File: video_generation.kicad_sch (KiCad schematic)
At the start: 53 parts, among them J12 28L22, J13 74LS86, J14 74LS166, J15 74LS161, K0000 74LS00, K10 74LS08, K11 74LS273, K12 74LS273, K14 74LS10, K15 74LS04, U14 74LS00, U2 74LS32, U3 74LS08, U4 74LS04, U5 74LS00

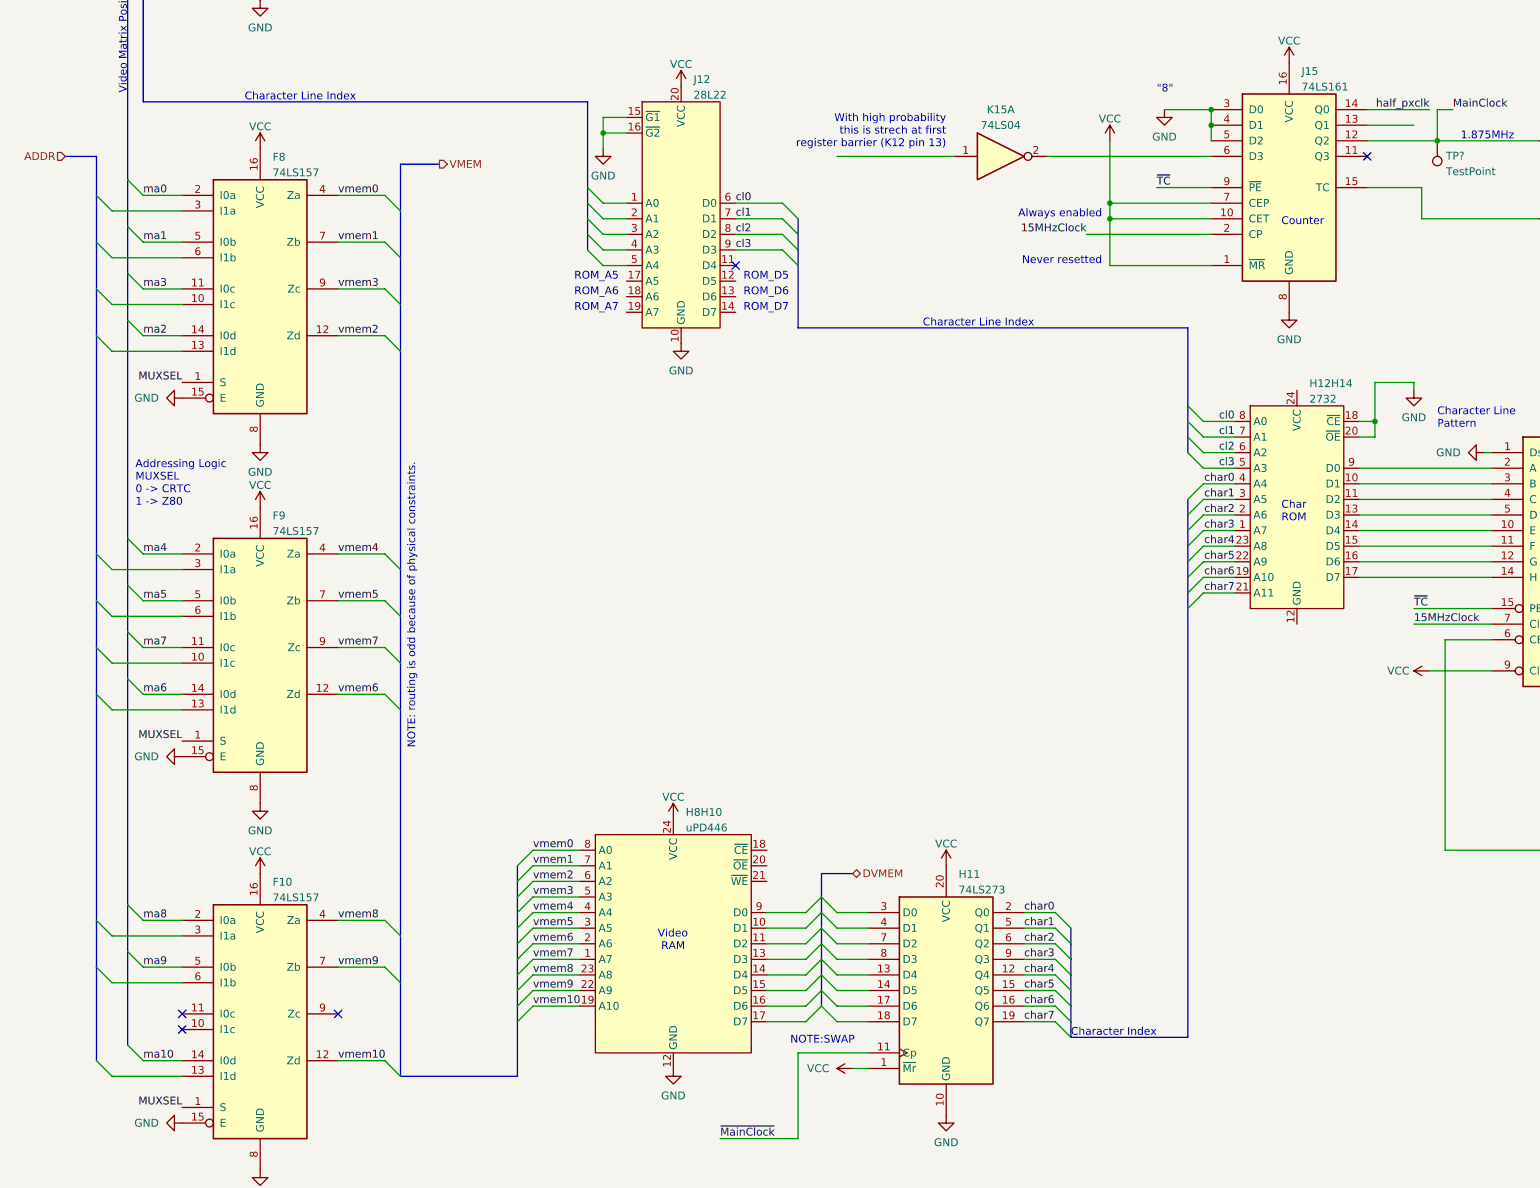
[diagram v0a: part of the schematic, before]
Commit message: Discovered WE and OE signals for video memories, plus others
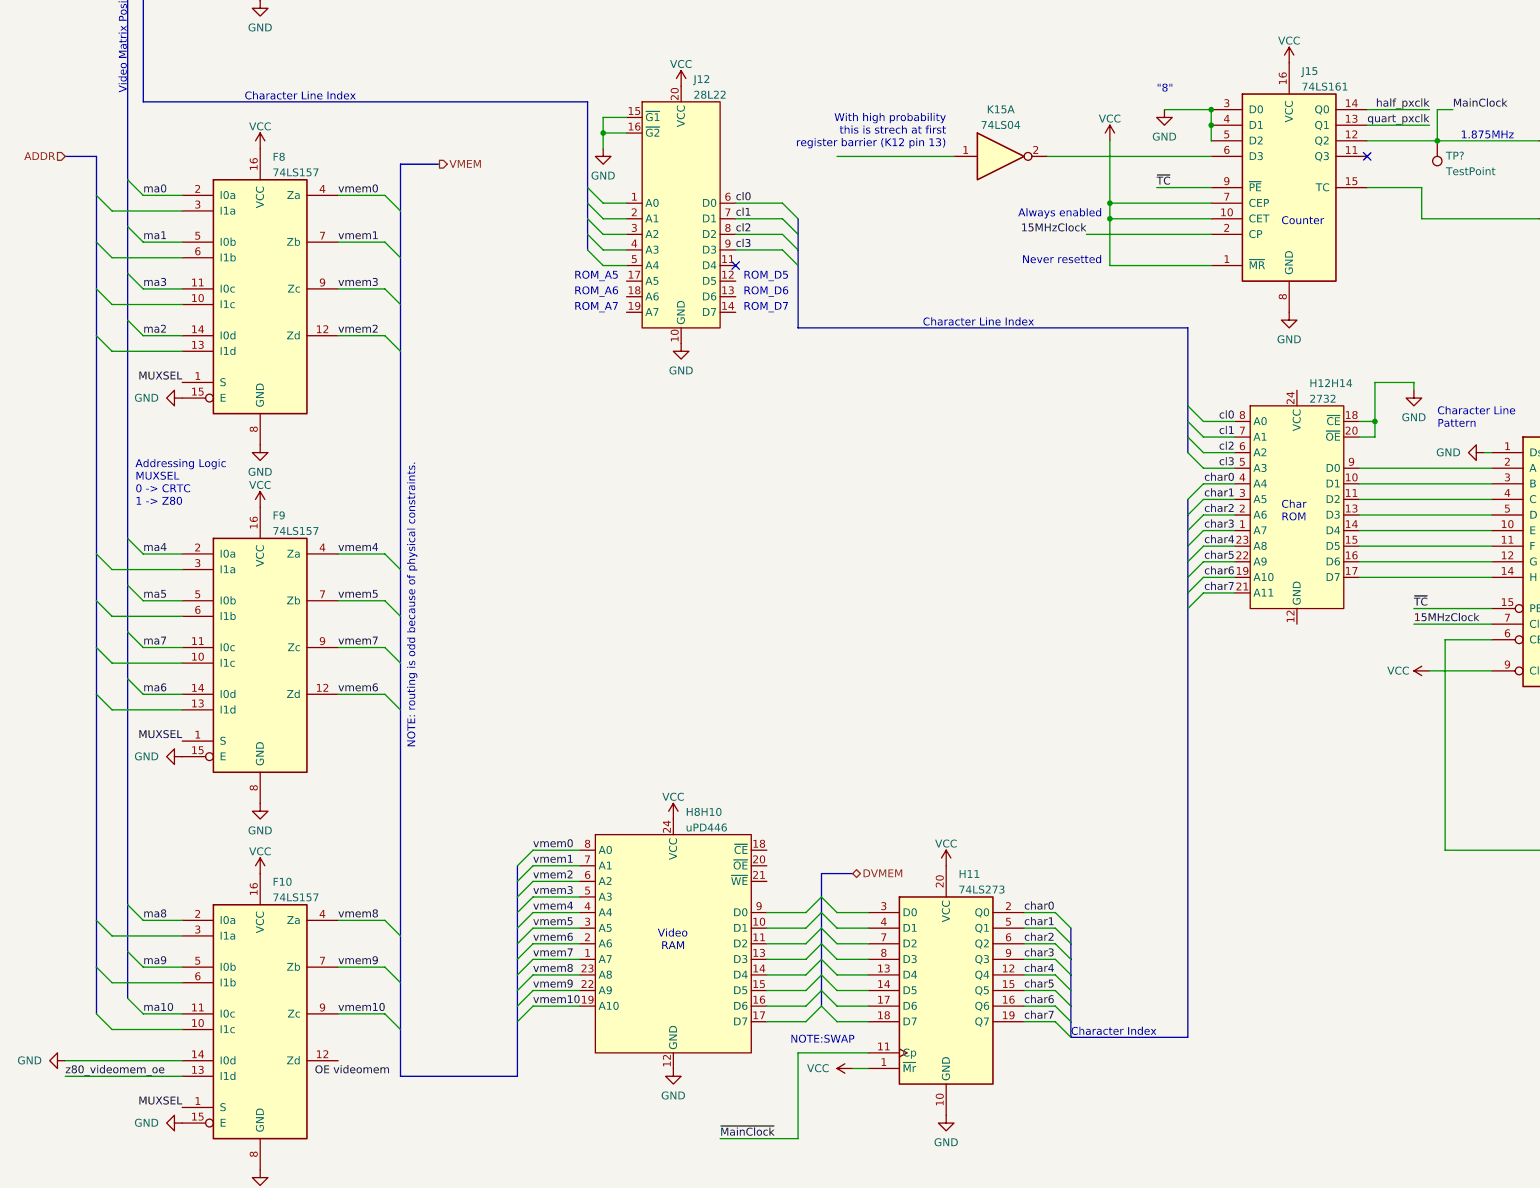
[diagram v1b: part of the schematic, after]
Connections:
- net GND: now also F10.14 (I0d)
- net ma10: now also F10.11 (I0c); no longer F10.14 (I0d)
- net vmem10: now also F10.9 (Zc); no longer F10.12 (Zd)
- net quart_pxclk: now reaches J15.13 (Q1)
- net z80_videomem_oe: now reaches F10.13 (I1d)
- no-connect marks 30 -> 27
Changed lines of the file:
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@@
   (no_connect (at 252.73 34.29))
   (no_connect (at 265.43 29.21))
-  (no_connect (at 39.37 256.54))
   (no_connect (at 374.65 143.51))
   (no_connect (at 495.3 228.6))
@@
   (no_connect (at 38.1 62.23))
   (no_connect (at 38.1 59.69))
-  (no_connect (at 64.77 254))
-  (no_connect (at 39.37 254))
   (no_connect (at 458.47 226.06))
   (no_connect (at 458.47 231.14))
@@
     (stroke (width 0) (type default))
   )
-  (bus_entry (at 72.39 261.62) (size 2.54 2.54)
+  (bus_entry (at 72.39 254) (size 2.54 2.54)
     (stroke (width 0) (type default))
   )
@@
     (stroke (width 0) (type default))
   )
-  (bus_entry (at 30.48 259.08) (size 2.54 2.54)
+  (bus_entry (at 30.48 251.46) (size 2.54 2.54)
     (stroke (width 0) (type default))
   )
@@
     (stroke (width 0) (type default))
   )
-  (bus_entry (at 25.4 261.62) (size 2.54 2.54)
+  (bus_entry (at 25.4 254) (size 2.54 2.54)
     (stroke (width 0) (type default))
   )
@@
     (stroke (width 0) (type default))
   )
-  (wire (pts (xy 27.94 264.16) (xy 39.37 264.16))
+  (wire (pts (xy 27.94 256.54) (xy 39.37 256.54))
     (stroke (width 0) (type default))
   )
@@
     (stroke (width 0) (type default))
   )
-  (wire (pts (xy 64.77 261.62) (xy 72.39 261.62))
+  (wire (pts (xy 64.77 254) (xy 72.39 254))
     (stroke (width 0) (type default))
   )
@@
     (stroke (width 0) (type default))
   )
-  (bus (pts (xy 30.48 243.84) (xy 30.48 259.08))
+  (bus (pts (xy 30.48 243.84) (xy 30.48 251.46))
     (stroke (width 0) (type default))
   )
@@
     (stroke (width 0) (type default))
   )
+  (bus (pts (xy 74.93 256.54) (xy 74.93 264.16))
+    (stroke (width 0) (type default))
+  )
   (wire (pts (xy 231.14 180.34) (xy 252.73 180.34))
     (stroke (width 0) (type default))
@@
     (stroke (width 0) (type default))
   )
-  (bus (pts (xy 74.93 248.92) (xy 74.93 264.16))
+  (bus (pts (xy 74.93 248.92) (xy 74.93 256.54))
     (stroke (width 0) (type default))
   )
@@
     (stroke (width 0) (type default))
   )
+  (wire (pts (xy 20.32 261.62) (xy 39.37 261.62))
+    (stroke (width 0) (type default))
+  )
   (wire (pts (xy 33.02 41.91) (xy 38.1 41.91))
     (stroke (width 0) (type default))
@@
     (stroke (width 0) (type default))
   )
-  (wire (pts (xy 33.02 261.62) (xy 39.37 261.62))
+  (wire (pts (xy 33.02 254) (xy 39.37 254))
     (stroke (width 0) (type default))
   )
@@
     (stroke (width 0) (type default))
   )
+  (wire (pts (xy 20.32 264.16) (xy 39.37 264.16))
+    (stroke (width 0) (type default))
+  )
   (wire (pts (xy 107.95 129.54) (xy 111.76 129.54))
     (stroke (width 0) (type default))
@@
     (stroke (width 0) (type default))
   )
-  (wire (pts (xy 232.41 109.22) (xy 240.03 109.22))
+  (wire (pts (xy 232.41 109.22) (xy 242.57 109.22))
     (stroke (width 0) (type default))
   )
@@
     (stroke (width 0) (type default))
   )
-  (bus (pts (xy 25.4 246.38) (xy 25.4 261.62))
+  (bus (pts (xy 25.4 246.38) (xy 25.4 254))
     (stroke (width 0) (type default))
   )
@@
     (effects (font (size 1.27 1.27)) (justify left bottom))
   )
-  (label "vmem10" (at 64.77 261.62 0) (fields_autoplaced)
+  (label "vmem10" (at 64.77 254 0) (fields_autoplaced)
     (effects (font (size 1.27 1.27)) (justify left bottom))
   )
@@
     (effects (font (size 1.27 1.27)) (justify left bottom))
   )
+  (label "OE videomem" (at 60.96 264.16 0) (fields_autoplaced)
+    (effects (font (size 1.27 1.27)) (justify left bottom))
+  )
   (label "CONTRAST1" (at 247.65 21.59 180) (fields_autoplaced)
     (effects (font (size 1.27 1.27)) (justify right bottom))
@@
     (effects (font (size 1.27 1.27)) (justify left bottom))
   )
+  (label "quart_pxclk" (at 242.57 109.22 180) (fields_autoplaced)
+    (effects (font (size 1.27 1.27)) (justify right bottom))
+  )
   (label "cl0" (at 36.83 69.85 180) (fields_autoplaced)
     (effects (font (size 1.27 1.27)) (justify right bottom))
   )
-  (label "ma10" (at 33.02 261.62 0) (fields_autoplaced)
+  (label "ma10" (at 33.02 254 0) (fields_autoplaced)
+    (effects (font (size 1.27 1.27)) (justify left bottom))
+  )
+  (label "z80_videomem_oe" (at 20.32 264.16 0) (fields_autoplaced)
     (effects (font (size 1.27 1.27)) (justify left bottom))
   )
@@
         )
       )
+    )
+  )
+  (symbol (lib_id "power:GND") (at 20.32 261.62 270) (unit 1)
+    (in_bom yes) (on_board yes) (dnp no)
+    (property "Reference" "#PWR0114" (at 13.97 261.62 0)
+      (effects (font (size 1.27 1.27)) hide)
+    )
+    (property "Value" "GND" (at 16.51 261.62 90)
+      (effects (font (size 1.27 1.27)) (justify right))
+    )
+    (property "Footprint" "" (at 20.32 261.62 0)
+      (effects (font (size 1.27 1.27)) hide)
+    )
+    (property "Datasheet" "" (at 20.32 261.62 0)
+      (effects (font (size 1.27 1.27)) hide)
+    )
+    (pin "1")
+    (instances
+      (project "ceda"
+        (path "/12a6dbe3-008d-4c5b-88f6-9f1c816060be/ce60e45b-d802-4380-8f39-bef3de5fa20e"
+          (reference "#PWR0114") (unit 1)
+        )
+      )

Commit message: Schematics refactoring:
- New sheet reserved to video memory.
- Removed video memory parts inside video_generation.
- Removed video memory parts inside GPIO.
- Generic cleanup to keep all circuits inside each sheet.
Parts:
- removed F10, F8, F9: 74LS157, symbol 74xx:74LS157
- removed H8H10: uPD446, symbol ceda:uPD446
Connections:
- net muxsel is gone; now on net MUXSEL: E12.9 (Cp)
- net dot pattern: now also J14.13 (Qh)
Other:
- note removed: ""8""
- note removed: "Addressing Logic MUXSEL 0 -> CRTC 1 -> Z80"
- note removed: "Character Index"
- note removed: "NOTE: routing is odd because of physical constraints."
- note removed: "TODO: feedback network is missing. Circuit must be something like as dashed lines"
- note removed: "Video Matrix Position"
- note removed: "Video RAM"
- moved on the sheet: C52, C53, C54, D2, D5, E12, H11, H12H14, J12, J13A, J13B, J14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

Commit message: Removed some dangling notes
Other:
- note removed: "Dot Pattern"
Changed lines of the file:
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@@
     (stroke (width 0) (type default))
   )
-  (bus_entry (at 66.04 167.64) (size 2.54 2.54)
-    (stroke (width 0) (type default))
-  )
-  (bus_entry (at 66.04 165.1) (size 2.54 2.54)
-    (stroke (width 0) (type default))
-  )
-  (bus_entry (at 66.04 172.72) (size 2.54 2.54)
-    (stroke (width 0) (type default))
-  )
-  (bus_entry (at 66.04 170.18) (size 2.54 2.54)
-    (stroke (width 0) (type default))
-  )
-  (bus_entry (at 66.04 162.56) (size 2.54 2.54)
-    (stroke (width 0) (type default))
-  )
-  (bus_entry (at 66.04 175.26) (size 2.54 2.54)
+  (bus_entry (at 68.58 167.64) (size 2.54 2.54)
+    (stroke (width 0) (type default))
+  )
+  (bus_entry (at 68.58 165.1) (size 2.54 2.54)
+    (stroke (width 0) (type default))
+  )
+  (bus_entry (at 68.58 172.72) (size 2.54 2.54)
+    (stroke (width 0) (type default))
+  )
+  (bus_entry (at 68.58 170.18) (size 2.54 2.54)
+    (stroke (width 0) (type default))
+  )
+  (bus_entry (at 68.58 162.56) (size 2.54 2.54)
+    (stroke (width 0) (type default))
+  )
+  (bus_entry (at 68.58 175.26) (size 2.54 2.54)
     (stroke (width 0) (type default))
   )
@@
     (stroke (width 0) (type default))
   )
-  (bus_entry (at 66.04 180.34) (size 2.54 2.54)
-    (stroke (width 0) (type default))
-  )
-  (bus_entry (at 66.04 177.8) (size 2.54 2.54)
+  (bus_entry (at 68.58 180.34) (size 2.54 2.54)
+    (stroke (width 0) (type default))
+  )
+  (bus_entry (at 68.58 177.8) (size 2.54 2.54)
     (stroke (width 0) (type default))
   )
@@
     (stroke (width 0) (type default))
   )
-  (wire (pts (xy 60.96 167.64) (xy 66.04 167.64))
+  (wire (pts (xy 60.96 167.64) (xy 68.58 167.64))
     (stroke (width 0) (type default))
   )
@@
     (stroke (width 0) (type default))
   )
-  (bus (pts (xy 68.58 172.72) (xy 68.58 175.26))
+  (bus (pts (xy 71.12 172.72) (xy 71.12 175.26))
     (stroke (width 0) (type default))
   )
@@
     (stroke (width 0) (type default))
   )
-  (wire (pts (xy 60.96 170.18) (xy 66.04 170.18))
+  (wire (pts (xy 60.96 170.18) (xy 68.58 170.18))
     (stroke (width 0) (type default))
   )
@@
     (stroke (width 0) (type default))
   )
-  (wire (pts (xy 60.96 172.72) (xy 66.04 172.72))
+  (wire (pts (xy 60.96 172.72) (xy 68.58 172.72))
     (stroke (width 0) (type default))
   )
@@
     (stroke (width 0) (type default))
   )
-  (bus (pts (xy 68.58 175.26) (xy 68.58 177.8))
+  (bus (pts (xy 71.12 175.26) (xy 71.12 177.8))
     (stroke (width 0) (type default))
   )
@@
     (stroke (width 0) (type default))
   )
-  (wire (pts (xy 60.96 165.1) (xy 66.04 165.1))
-    (stroke (width 0) (type default))
-  )
-  (wire (pts (xy 60.96 177.8) (xy 66.04 177.8))
+  (wire (pts (xy 60.96 165.1) (xy 68.58 165.1))
+    (stroke (width 0) (type default))
+  )
+  (wire (pts (xy 60.96 177.8) (xy 68.58 177.8))
     (stroke (width 0) (type default))
   )
@@
     (stroke (width 0) (type default))
   )
-  (bus (pts (xy 68.58 170.18) (xy 68.58 172.72))
+  (bus (pts (xy 71.12 170.18) (xy 71.12 172.72))
     (stroke (width 0) (type default))
   )
@@
     (stroke (width 0) (type default))
   )
-  (bus (pts (xy 68.58 180.34) (xy 68.58 182.88))
+  (bus (pts (xy 71.12 180.34) (xy 71.12 182.88))
     (stroke (width 0) (type default))
   )
@@
     (stroke (width 0) (type default))
   )
-  (wire (pts (xy 60.96 162.56) (xy 66.04 162.56))
+  (wire (pts (xy 60.96 162.56) (xy 68.58 162.56))
     (stroke (width 0) (type default))
   )
@@
     (stroke (width 0) (type default))
   )
-  (bus (pts (xy 68.58 165.1) (xy 68.58 167.64))
+  (bus (pts (xy 71.12 165.1) (xy 71.12 167.64))
     (stroke (width 0) (type default))
   )
@@
     (stroke (width 0) (type default))
   )
-  (bus (pts (xy 71.12 156.21) (xy 71.12 154.94))
+  (bus (pts (xy 71.12 154.94) (xy 71.12 165.1))
     (stroke (width 0) (type default))
   )
@@
     (stroke (width 0) (type default))
   )
-  (bus (pts (xy 68.58 156.21) (xy 68.58 165.1))
-    (stroke (width 0) (type default))
-  )
   (bus (pts (xy 73.66 67.31) (xy 73.66 64.77))
     (stroke (width 0) (type default))
@@
     (stroke (width 0) (type default))
   )
-  (bus (pts (xy 68.58 167.64) (xy 68.58 170.18))
+  (bus (pts (xy 71.12 167.64) (xy 71.12 170.18))
     (stroke (width 0) (type default))
   )
@@
     (stroke (width 0) (type default))
   )
-  (wire (pts (xy 60.96 180.34) (xy 66.04 180.34))
+  (wire (pts (xy 60.96 180.34) (xy 68.58 180.34))
     (stroke (width 0) (type default))
   )
@@
     (stroke (width 0) (type default))
   )
-  (bus (pts (xy 71.12 156.21) (xy 68.58 156.21))
-    (stroke (width 0) (type default))
-  )
   (bus (pts (xy 33.02 80.01) (xy 33.02 82.55))
     (stroke (width 0) (type default))
@@
     (stroke (width 0) (type default))
   )
-  (bus (pts (xy 68.58 177.8) (xy 68.58 180.34))
+  (bus (pts (xy 71.12 177.8) (xy 71.12 180.34))
     (stroke (width 0) (type default))
   )
@@
     (stroke (width 0) (type default))
   )
-  (wire (pts (xy 60.96 175.26) (xy 66.04 175.26))
+  (wire (pts (xy 60.96 175.26) (xy 68.58 175.26))
     (stroke (width 0) (type default))
   )
@@
     (effects (font (size 1.27 1.27)) (justify left bottom))
   )
-  (text "Character Line Index" (at 71.12 133.35 90)
+  (text "Character Line Index" (at 60.96 115.57 0)
     (effects (font (size 1.27 1.27)) (justify left bottom))
   )
@@
     (effects (font (size 1.27 1.27)) (justify left bottom))
   )
-  (text "Dot Pattern" (at 270.51 95.25 0)
-    (effects (font (size 1.27 1.27)) (justify left bottom))
-  )

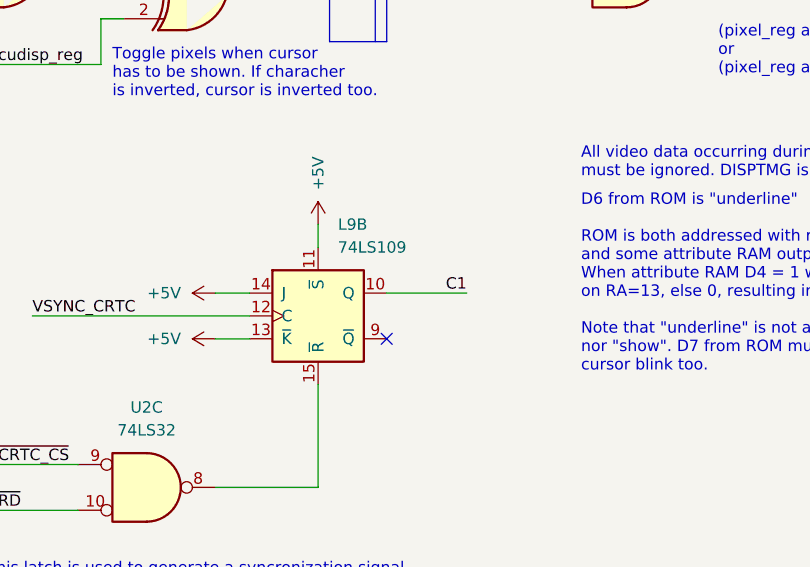
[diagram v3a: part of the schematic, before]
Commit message: GPIO: wire renaming
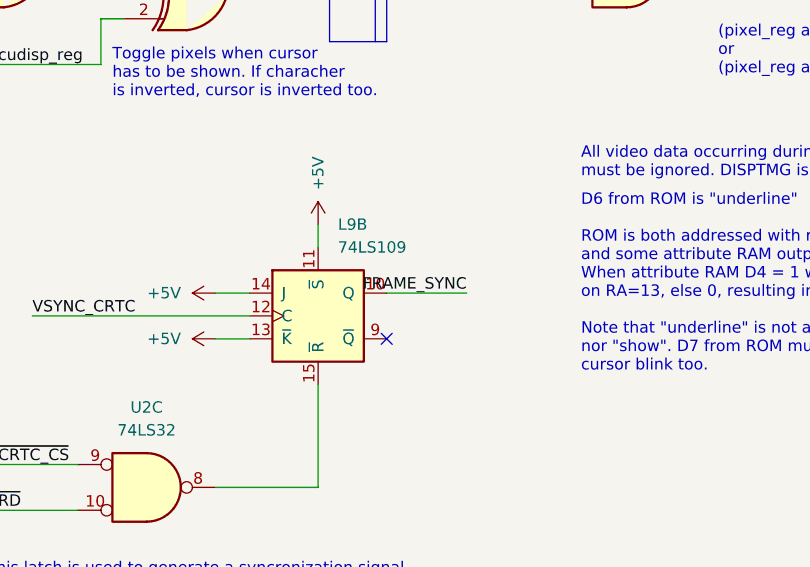
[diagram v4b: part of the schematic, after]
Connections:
- net C1 renamed FRAME_SYNC
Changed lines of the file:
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@@
     (effects (font (size 1.27 1.27)) (justify left bottom))
   )
-  (label "C1" (at 284.48 177.8 180) (fields_autoplaced)
+  (label "FRAME_SYNC" (at 284.48 177.8 180) (fields_autoplaced)
     (effects (font (size 1.27 1.27)) (justify right bottom))
   )
